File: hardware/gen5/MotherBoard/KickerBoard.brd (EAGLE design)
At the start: 143.9 x 149.3 mm, 193 parts, among them U1 SAM3S4B

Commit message: small edits
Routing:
- net M1QA-3: track 81.5 -> 64.7 mm, vias 4 -> 2
- net BREN2: track 76.5 -> 74.0 mm
- net INT2: track 71.6 -> 69.7 mm

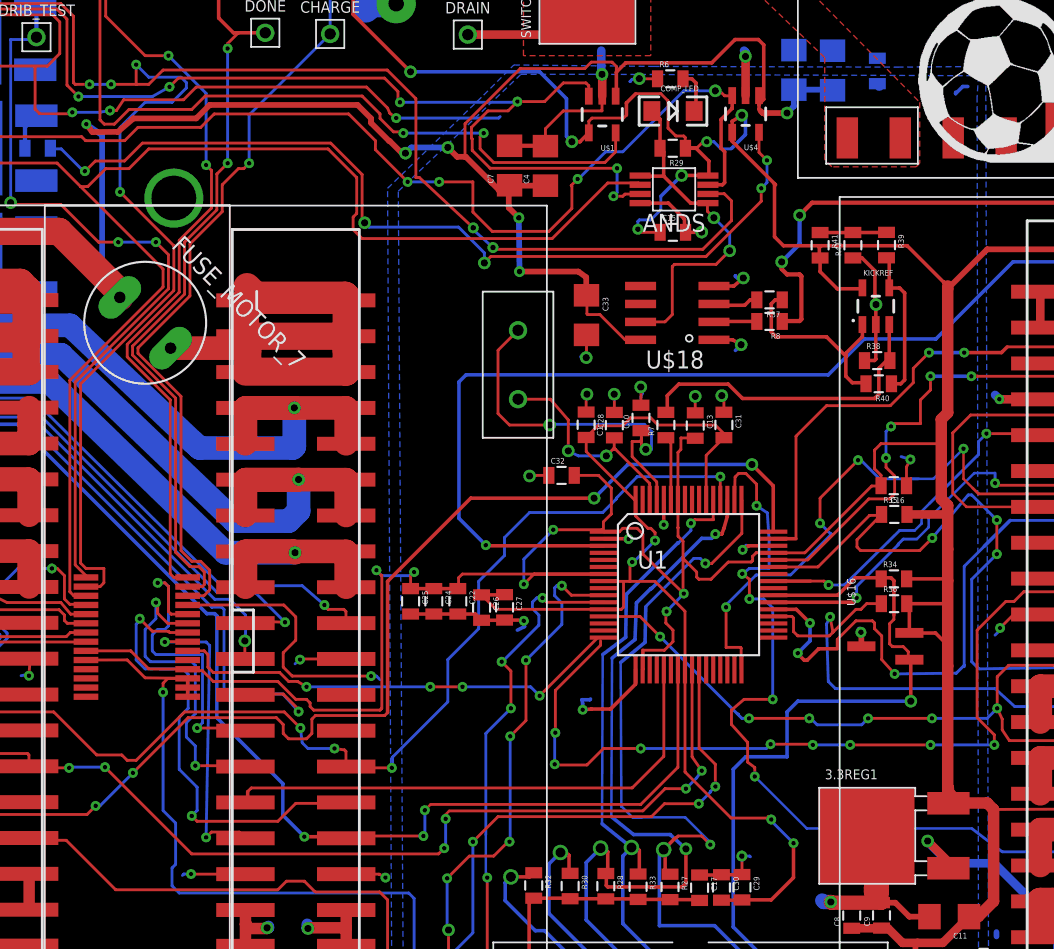
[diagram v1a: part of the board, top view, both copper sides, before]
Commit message: added two more wires to left multiplexer
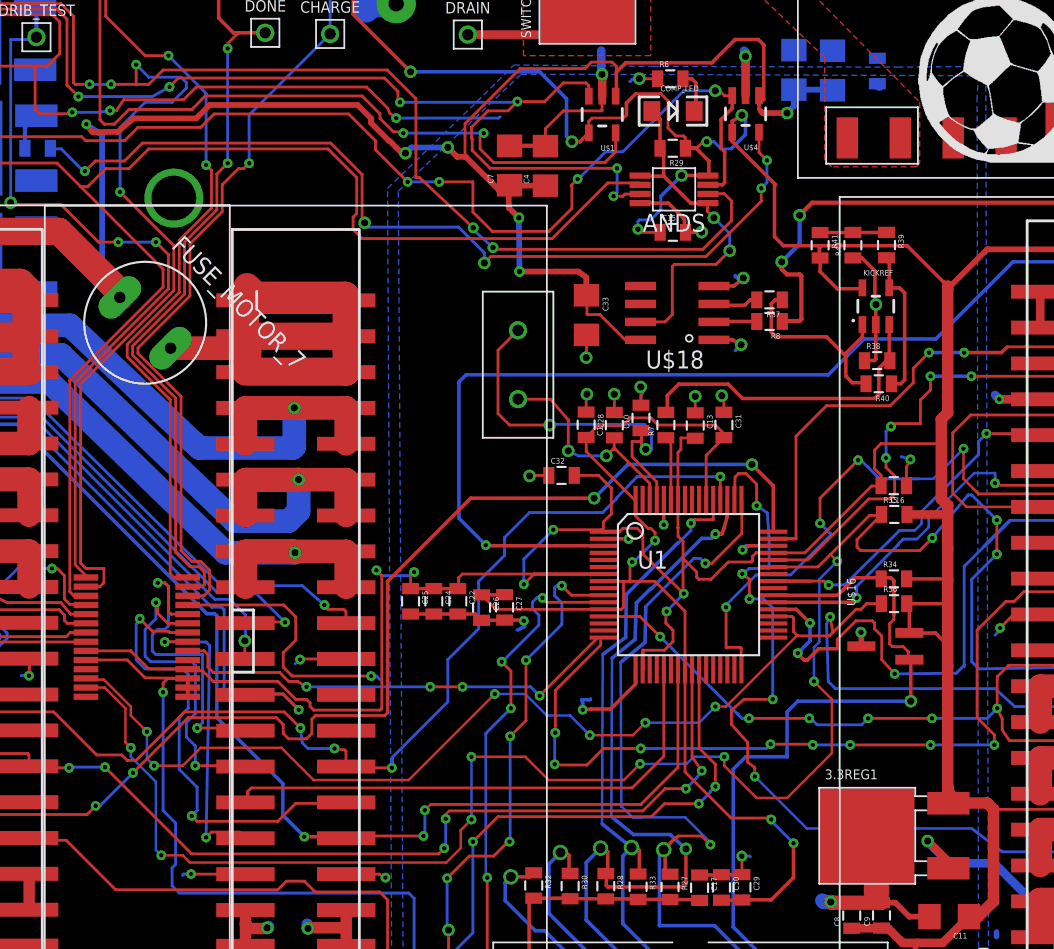
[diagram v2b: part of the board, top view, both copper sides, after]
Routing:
- net TWD: track 54.9 -> 143.7 mm, vias 4 -> 12
- net TWCK: track 46.3 -> 108.9 mm, vias 2 -> 8
- net GND: track 433.1 -> 431.9 mm

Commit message: improved ground connections near left side motor, added 5V regulator,comms i2c lines, and cleaned up a bit. Almost there
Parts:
- removed 5V1: TEST_PT, gen3:TESTING_PT
- moved C39 201.4 mm to (6.25, 26.0), flipped to the bottom, turned to 180 degrees
- moved C40 200.7 mm to (6.25, 27.7), flipped to the bottom, turned to 180 degrees
- moved C41 48.8 mm to (5.33, 24.2), turned to 180 degrees
- moved 5REG3 45.5 mm to (11.4, 25.4), turned to 270 degrees
- moved U$20 0.39 mm to (47.6, 17.3), flipped to the bottom, turned to 180 degrees
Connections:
- net 5V: no longer 5V1.P$1
- net M1QA-2: no longer JP1.3, MOTOR2.28
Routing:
- net 5V: track 0.00 -> 277.4 mm, vias 0 -> 7
- net GND: track 431.9 -> 490.6 mm, vias 30 -> 32
- net TWCK: track 108.9 -> 149.6 mm, vias 8 -> 12
- net TWD: track 143.7 -> 180.3 mm, vias 12 -> 15
- net 3.3V: track 629.6 -> 659.5 mm, vias 19 -> 22
- net BATSENSE: track 131.2 -> 159.0 mm, vias 2 -> 7
- net M1QA-3: track 64.7 -> 81.8 mm, vias 2 -> 4
- net N$27: track 65.4 -> 56.6 mm
- net CHARGE: track 80.3 -> 87.7 mm
- net 12V: track 630.4 -> 637.6 mm, vias 8 -> 9
- net N$69: track 57.5 -> 50.3 mm
- net 12VGND: track 291.8 -> 284.8 mm, vias 33 -> 32
- net INT1: track 32.5 -> 38.7 mm, vias 4 -> 2
- net CHIP_ENABLE: track 124.8 -> 130.9 mm
- net N$1: track 9.61 -> 3.89 mm
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- added copper zone on layer 1, net 12VGND

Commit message: Voltage Dividers Installed
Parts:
- removed KICKREF1, KICKREF2, KICKREF3, KICKREF4, KICKREF5, KICKREF6, KICKREF7, KICKREF8: MCP6291T-E/OT, SparkFun-AnalogIC:SOT23-5
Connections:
- removed net 5V1: KICKREF2.5
- removed net 5V2: KICKREF3.5
- removed net 5V3: KICKREF4.5
- removed net 5V4: KICKREF5.5
- removed net 5V5: KICKREF6.5
- removed net 5V6: KICKREF7.5
- removed net 5V7: KICKREF8.5
- removed net GND1: KICKREF2.2
- removed net GND2: KICKREF3.2
- removed net GND3: KICKREF4.2
- removed net GND4: KICKREF5.2
- removed net GND5: KICKREF6.2
- removed net GND6: KICKREF7.2
- removed net GND7: KICKREF8.2
- removed net N$33: KICKREF1.3, R44.1, R45.1
- removed net N$62: R44.2
- removed net N$63: KICKREF1.1, KICKREF1.4
- removed net N$64: KICKREF2.3, R46.1, R47.1
- removed net N$73: R46.2
- removed net N$74: KICKREF2.1, KICKREF2.4
- removed net N$75: KICKREF3.3, R48.1, R49.1
- removed net N$76: R48.2
- removed net N$77: KICKREF3.1, KICKREF3.4
- removed net N$78: KICKREF4.3, R50.1, R51.1
- removed net N$79: R50.2
- removed net N$80: KICKREF4.1, KICKREF4.4
- removed net N$81: KICKREF5.3, R52.1, R53.1
- removed net N$82: R52.2
- removed net N$83: KICKREF5.1, KICKREF5.4
- removed net N$84: KICKREF6.3, R54.1, R55.1
- removed net N$85: R54.2
- removed net N$86: KICKREF6.1, KICKREF6.4
- removed net N$87: KICKREF7.3, R56.1, R57.1
- removed net N$88: R56.2
- removed net N$89: KICKREF7.1, KICKREF7.4
- removed net N$90: KICKREF8.3, R58.1, R59.1
- removed net N$91: R58.2
- removed net N$92: KICKREF8.1, KICKREF8.4
- new net M1QA-1OUT: R58.1, R59.1, U1.25
- new net M1QA-2OUT: R52.1, R53.1, U1.37
- new net M1QA-3OUT: R54.1, R55.1, U1.42
- new net M1QA-4OUT: R56.1, R57.1, U1.52
- new net M1QB-1OUT: R50.1, R51.1, U1.26
- new net M1QB-2OUT: R44.1, R45.1, U1.38
- new net M1QB-3OUT: R46.1, R47.1, U1.41
- new net M1QB-4OUT: R48.1, R49.1, U1.23
- net 5V: no longer KICKREF1.5
- net GND: now also R45.2, R47.2, R49.2, R51.2, R53.2, R55.2, R57.2, R59.2; no longer KICKREF1.2
- net M1QA-1: now also R58.2; no longer MOTOR1.28, U1.25
- net M1QA-2: now also JP1.3, R52.2; no longer U1.37
- net M1QA-3: now also R54.2; no longer MOTOR3.28, U1.42
- net M1QA-4: now also R56.2; no longer MOTOR4.28, U1.52
- net M1QB-1: now also R50.2; no longer MOTOR1.32, U1.26
- net M1QB-2: now also R44.2; no longer MOTOR2.32, U1.38
- net M1QB-3: now also R46.2; no longer MOTOR3.32, U1.41
- net M1QB-4: now also R48.2; no longer MOTOR4.32, U1.23
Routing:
- net M1QB-1: track 102.5 -> 0.00 mm, vias 4 -> 0
- net M1QB-1OUT: track 0.00 -> 101.2 mm, vias 0 -> 4
- net M1QA-2: track 95.2 -> 0.00 mm, vias 6 -> 0
- net M1QB-4: track 93.2 -> 0.00 mm, vias 4 -> 0
- net M1QA-2OUT: track 0.00 -> 89.5 mm, vias 0 -> 6
- net M1QA-4: track 88.6 -> 0.00 mm, vias 2 -> 0
- net M1QB-2: track 83.5 -> 0.00 mm, vias 4 -> 0
- net M1QA-1: track 78.3 -> 0.00 mm, vias 6 -> 0
- net M1QB-3: track 75.1 -> 0.00 mm, vias 4 -> 0
- net M1QA-1OUT: track 0.00 -> 65.1 mm, vias 0 -> 6
- net M1QB-2OUT: track 0.00 -> 60.7 mm, vias 0 -> 4
- net M1QA-4OUT: track 0.00 -> 42.2 mm, vias 0 -> 2
- net M1QB-4OUT: track 0.00 -> 33.3 mm, vias 0 -> 2
- net M1QB-3OUT: track 0.00 -> 24.4 mm, vias 0 -> 2
- net M1QA-3: track 81.8 -> 71.3 mm
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
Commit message: Added mosfet on motherboard
new mosfet (2N7002K-T1-E3) in library and added to comp_led circuitry
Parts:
- added U$22: N-FET, rfc:SOT-23
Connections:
- new net N$14: R6.1, U$22.D
- net 3.3V: now also COMP_LED.A
- net COMP_OUT: now also U$22.G; no longer COMP_LED.A
- net GND: now also U$22.S; no longer R6.1
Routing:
- net N$14: track 0.00 -> 11.3 mm
- net COMP_OUT: track 25.2 -> 33.3 mm
- net 12V: track 637.6 -> 643.7 mm
- net GND: track 488.7 -> 489.3 mm
- net 3.3V: track 659.5 -> 660.0 mm, vias 22 -> 23

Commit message: finishing
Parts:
- moved C36 192.8 mm to (28.4, 54.5)
- moved C35 189.3 mm to (28.4, 52.7)
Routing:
- net GND: track 489.3 -> 506.4 mm, vias 32 -> 34
- net 3.3V: track 660.0 -> 670.7 mm
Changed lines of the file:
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@@
 <element name="R43" library="SparkFun-Passives" package="0805" value="100" x="61.087" y="95.25" rot="R270"/>
 <element name="U$17" library="Kicker" package="SSOP" value="IO-EXPANDER" x="25.527" y="48.133" rot="R270"/>
-<element name="C35" library="SparkFun-Capacitors" package="0805" value="100nF" x="-123.952" y="-59.69"/>
-<element name="C36" library="SparkFun-Capacitors" package="0805" value="2.2uF" x="-127" y="-59.69"/>
+<element name="C35" library="SparkFun-Capacitors" package="0805" value="100nF" x="28.4226" y="52.6796"/>
+<element name="C36" library="SparkFun-Capacitors" package="0805" value="2.2uF" x="28.3972" y="54.4576"/>
 <element name="U$21" library="Kicker" package="SSOP" value="IO-EXPANDER" x="112.014" y="38.862" rot="R180"/>
 <element name="C37" library="SparkFun-Capacitors" package="0805" value="100nF" x="-127" y="-77.216"/>
@@
 <wire x1="25.6032" y1="42.3164" x2="24.3586" y2="42.3164" width="0.3048" layer="1"/>
 <wire x1="24.3586" y1="42.3164" x2="24.1808" y2="42.1386" width="0.3048" layer="1"/>
-<wire x1="24.1808" y1="42.1386" x2="24.1808" y2="38.7604" width="0.3048" layer="1"/>
+<wire x1="24.1808" y1="42.1386" x2="24.1808" y2="41.0718" width="0.3048" layer="1"/>
+<wire x1="24.1808" y1="41.0718" x2="24.1808" y2="38.7604" width="0.3048" layer="1"/>
 <wire x1="24.1808" y1="38.7604" x2="26.67" y2="36.2712" width="0.3048" layer="1"/>
 <via x="26.67" y="36.2712" extent="1-16" drill="0.3048"/>
@@
 <via x="69.342" y="83.9216" extent="1-16" drill="0.5"/>
 <wire x1="69.342" y1="83.9216" x2="69.342" y2="83.566" width="0.2032" layer="16"/>
+<wire x1="29.2972" y1="54.4576" x2="29.2972" y2="54.4466" width="0.3048" layer="1"/>
+<wire x1="29.2972" y1="54.4466" x2="29.337" y2="54.4068" width="0.3048" layer="1"/>
+<wire x1="29.337" y1="54.4068" x2="29.337" y2="52.694" width="0.3048" layer="1"/>
+<wire x1="29.337" y1="52.694" x2="29.3226" y2="52.6796" width="0.3048" layer="1"/>
+<wire x1="29.3226" y1="52.6796" x2="29.3226" y2="48.1694" width="0.254" layer="1"/>
+<wire x1="29.3226" y1="48.1694" x2="28.448" y2="47.2948" width="0.254" layer="1"/>
+<via x="28.448" y="47.2948" extent="1-16" drill="0.3048"/>
+<wire x1="28.448" y1="47.2948" x2="28.448" y2="46.4058" width="0.254" layer="16"/>
+<wire x1="28.448" y1="46.4058" x2="23.114" y2="41.0718" width="0.254" layer="16"/>
+<via x="23.114" y="41.0718" extent="1-16" drill="0.3048"/>
+<wire x1="23.114" y1="41.0718" x2="24.1808" y2="41.0718" width="0.254" layer="1"/>
 <wire x1="-123.052" y1="-77.216" x2="-126.1" y2="-77.216" width="0" layer="19" extent="1-1"/>
-<wire x1="-126.1" y1="-59.69" x2="-126.1" y2="-77.216" width="0" layer="19" extent="1-1"/>
-<wire x1="-123.052" y1="-59.69" x2="-126.1" y2="-59.69" width="0" layer="19" extent="1-1"/>
 <wire x1="-135.371" y1="-124.968" x2="-126.1" y2="-77.216" width="0" layer="19" extent="1-1"/>
 <wire x1="-135.498" y1="-133.096" x2="-135.371" y2="-124.968" width="0" layer="19" extent="1-1"/>
@@
 <wire x1="-129.402" y1="-162.306" x2="-135.498" y2="-162.306" width="0" layer="19" extent="1-1"/>
 <wire x1="-129.402" y1="-159.004" x2="-129.402" y2="-162.306" width="0" layer="19" extent="1-1"/>
-<wire x1="6.734" y1="24.1554" x2="-123.052" y2="-59.69" width="0" layer="19" extent="1-16"/>
+<wire x1="6.734" y1="24.1554" x2="-123.052" y2="-77.216" width="0" layer="19" extent="1-16"/>
 <wire x1="130.25348125" y1="47.055534375" x2="128.331465625" y2="47.055534375" width="0" layer="19" extent="1-1"/>
 </signal>
@@
 <wire x1="64.7192" y1="78.0542" x2="66.167" y2="76.6064" width="0.2032" layer="16"/>
 <wire x1="66.167" y1="76.6064" x2="67.7164" y2="76.6064" width="0.2032" layer="16"/>
+<wire x1="27.5226" y1="52.6796" x2="27.5226" y2="43.9784" width="0.3048" layer="1"/>
+<wire x1="27.5226" y1="43.9784" x2="27.686" y2="43.815" width="0.3048" layer="1"/>
+<wire x1="27.4972" y1="54.4576" x2="27.4972" y2="52.705" width="0.3048" layer="1"/>
+<wire x1="27.4972" y1="52.705" x2="27.5226" y2="52.6796" width="0.3048" layer="1"/>
 <wire x1="-124.852" y1="-77.216" x2="-127.9" y2="-77.216" width="0" layer="19" extent="1-1"/>
-<wire x1="-127.9" y1="-59.69" x2="-127.9" y2="-77.216" width="0" layer="19" extent="1-1"/>
-<wire x1="-124.852" y1="-59.69" x2="-127.9" y2="-59.69" width="0" layer="19" extent="1-1"/>
-<wire x1="24.96639375" y1="26.21460625" x2="-124.852" y2="-59.69" width="0" layer="19" extent="1-16"/>
+<wire x1="24.96639375" y1="26.21460625" x2="-124.852" y2="-77.216" width="0" layer="19" extent="1-16"/>
 <wire x1="56.9147125" y1="20.051740625" x2="56.9147125" y2="17.5072875" width="0" layer="19" extent="1-1"/>
 </signal>

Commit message: routing encoder signals
routing encoder signals (voltage dividers)
almost done
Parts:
- moved R52 354.0 mm to (127.3, 73.7)
- moved R53 350.8 mm to (127.3, 72.3)
- moved R54 335.1 mm to (131.7, 45.9), flipped to the bottom, turned to 180 degrees
- moved R55 331.8 mm to (131.8, 44.5), flipped to the bottom, turned to 180 degrees
- moved R45 324.0 mm to (126.5, 64.6)
- moved R44 322.4 mm to (126.5, 66.0)
- moved R46 321.5 mm to (127.5, 45.9), flipped to the bottom
- moved R47 318.1 mm to (127.5, 44.5), flipped to the bottom
- moved R56 264.7 mm to (9.37, 56.6)
- moved R57 261.8 mm to (9.45, 55.1), turned to 180 degrees
- moved C37 258.4 mm to (109.0, 27.9), flipped to the bottom
- moved C38 256.3 mm to (109.0, 29.6), flipped to the bottom
- moved R58 242.5 mm to (9.60, 33.6), flipped to the bottom
- moved R49 240.2 mm to (9.60, 42.3), turned to 180 degrees
- moved R59 239.6 mm to (9.58, 32.2), flipped to the bottom
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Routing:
- net M1QA-4OUT: track 42.2 -> 91.6 mm
- net M1QB-4OUT: track 33.3 -> 78.0 mm
- net M1QA-4: track 0.00 -> 18.2 mm
- net M1QB-1OUT: track 101.2 -> 86.0 mm
- net M1QA-1OUT: track 65.1 -> 79.7 mm, vias 6 -> 7
- net M1QB-1: track 0.00 -> 14.4 mm
- net M1QB-4: track 0.00 -> 12.4 mm
- net GND: track 506.4 -> 494.9 mm, vias 34 -> 35
- net 3.3V: track 670.7 -> 677.3 mm, vias 23 -> 24
- net M1QA-1: track 0.00 -> 2.55 mm, vias 0 -> 1
- net FAULT1: track 108.3 -> 107.6 mm
- net 5V: track 277.4 -> 276.8 mm

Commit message: done
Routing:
- net M1QA-3OUT: track 0.00 -> 100.7 mm, vias 0 -> 3
- net GND: track 494.9 -> 549.4 mm, vias 35 -> 42
- net M1QB-3OUT: track 24.4 -> 74.2 mm, vias 2 -> 5
- net M1QB-2OUT: track 60.7 -> 79.1 mm
- net M1QA-3: track 71.3 -> 80.7 mm, vias 4 -> 5
- net M1QA-2: track 0.00 -> 9.25 mm, vias 0 -> 2
- net M1QB-3: track 0.00 -> 7.73 mm, vias 0 -> 1
- net M1QB-1OUT: track 86.0 -> 92.4 mm, vias 4 -> 6
- net M1QA-2OUT: track 89.5 -> 94.3 mm
- net M1QB-2: track 0.00 -> 3.99 mm
- net M1QB-1: track 14.4 -> 16.4 mm
